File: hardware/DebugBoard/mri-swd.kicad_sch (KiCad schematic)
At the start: 7 parts, among them J1 Debug UART/Power, J2 Debug SWD, J5 OLED, SW1 Reset, SW2 Halt on Connect, U1 PicoW

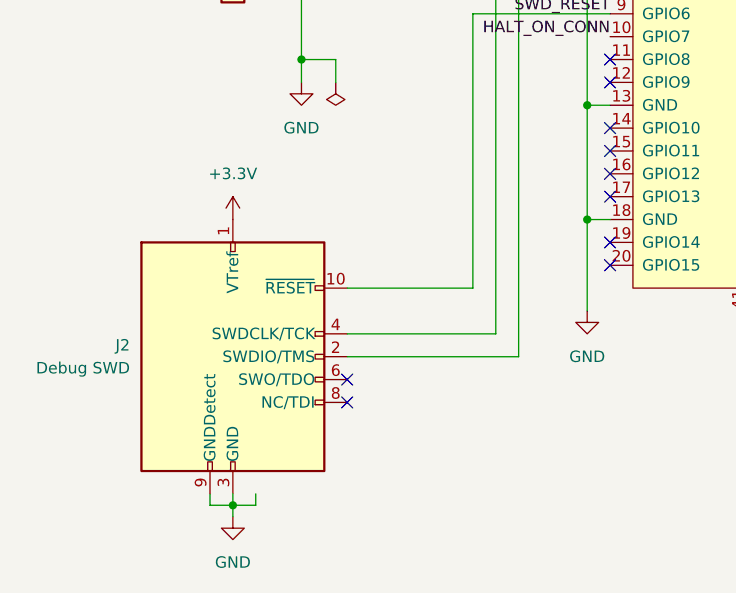
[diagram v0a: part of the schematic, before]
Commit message: Fixes to PCB found during Chomps bring up
I hit a few issues when attempting to use the mri-swd DebugBoard PCB
with the initial revision of my Chomps main board:
* The VTref pin of the SWD connector was connected to 3.3V on the debug
  board. This meant that both the target and the debugger were applying
  power to this bus. I now have the VTref pin of the SWD connector left
  unconnected. I hacked the same change into my already manufactured
  PCBs by cutting the trace leading away from the VTref pin.
* The nReset pin of the SWD connector is connected to the GPIO6 pin of
  the Pico with nothing else. This meant that nReset was connected to
  ground via the default ~50kohm pulldown of the debugger's RP2040
  and also pulled up by the default ~50kohm pull-up of the target's
  RP2040 so the voltage sits pretty close to the transition area which
  causes very weird behavior in the target and the debugger fails to
  successfully connect to the target via SWD. I added an external
  1kohm pull-up resistor to the debugger board to override the
  default pulldown behavior of the RP2040. I hacked the same change into
  my already manufactured PCBs by bodging in a 1kohm through hole
  resistor between the Pico's GPIO6 and 3.3V pins.

I bumped the version of the schematic and PCB up to 1.1 after these
changes were applied.
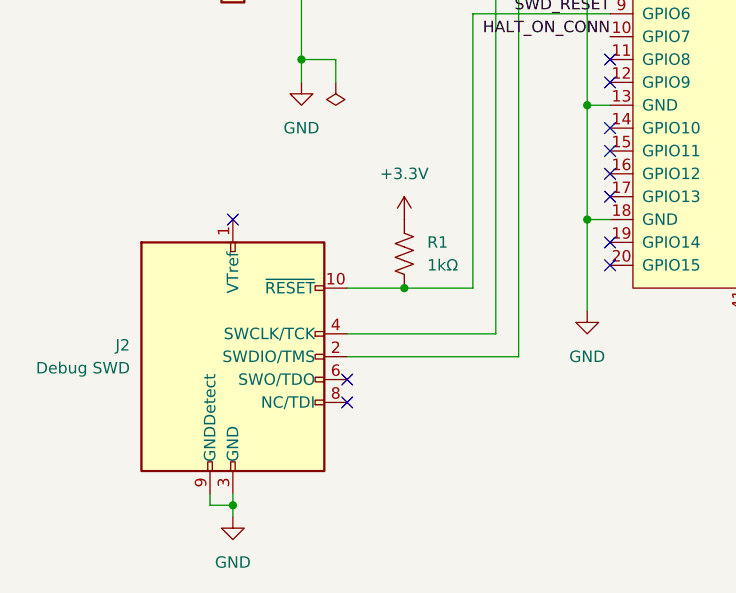
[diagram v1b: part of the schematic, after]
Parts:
- added R1: 1kΩ, Resistor_SMD:R_0805_2012Metric_Pad1.20x1.40mm_HandSolder, symbol Device:R_US
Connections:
- net +3.3V: now also R1.1; no longer J2.1 (VTref)
- net SWD_RESET: now also R1.2
- no-connect marks 25 -> 26

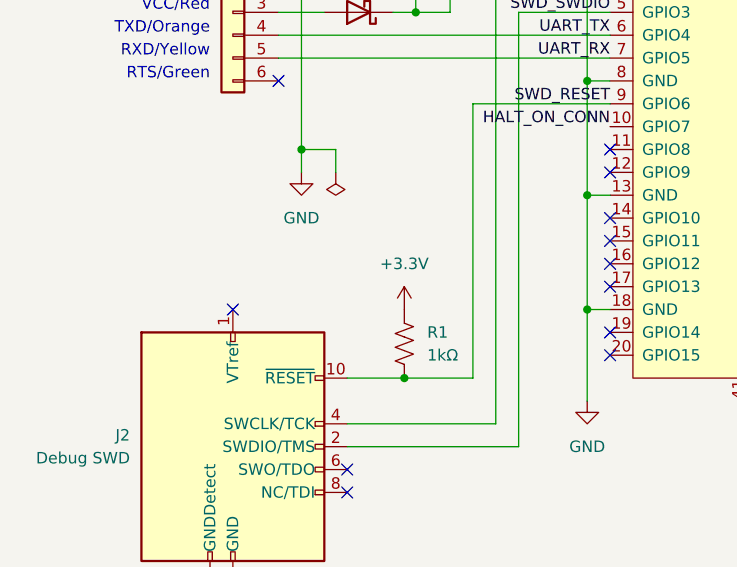
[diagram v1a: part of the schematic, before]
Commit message: More fixes to PCB found during Chomps bring up
I hit another issue when attempting to use the mri-swd DebugBoard PCB
with the initial revision of my Chomps main board:
* I previously added a 1kohm pull-up resistor to the nReset pin on the
  SWD connector but I connected it to the regulated 3.3V on the
  debugger board rather than the VTref pin on the SWD connector. This
  means that nReset wasn't pulled-up correctly if the debugger board
  wasn't powered up. Now it does the right thing even if the debugger
  board is connected to a target but hasn't been yet powered up.

I bumped the version of the schematic and PCB up to 1.2 after these
changes were applied.
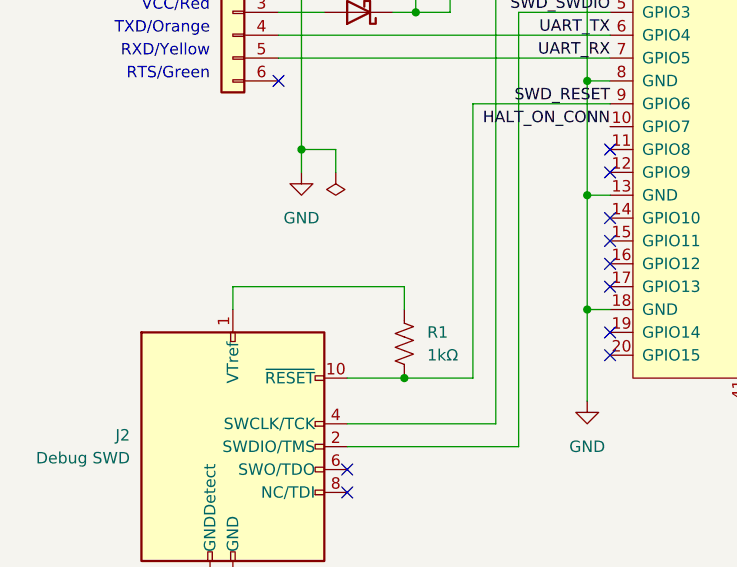
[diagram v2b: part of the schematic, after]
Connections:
- net +3.3V: no longer R1.1
- net at J2.1 (VTref): now also R1.1
- no-connect marks 26 -> 25
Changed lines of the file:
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@@
 	(title_block
 		(title "MRI SWD Hardware Debugger Board")
-		(date "2024-07-13")
+		(date "2024-07-28")
 		(rev "1.1")
 	)
@@
 		(at 147.32 90.17)
 	)
-	(no_connect
-		(at 69.85 100.33)
-	)
 	(wire
 		(pts
@@
 	(wire
 		(pts
+			(xy 69.85 100.33) (xy 69.85 97.79)
+		)
+		(stroke
+			(width 0)
+			(type default)
+		)
+	)
+	(wire
+		(pts
 			(xy 101.6 67.31) (xy 111.76 67.31)
 		)
@@
 		(pts
 			(xy 149.86 74.93) (xy 149.86 87.63)
+		)
+		(stroke
+			(width 0)
+			(type default)
+		)
+	)
+	(wire
+		(pts
+			(xy 88.9 97.79) (xy 88.9 100.33)
+		)
+		(stroke
+			(width 0)
+			(type default)
+		)
+	)
+	(wire
+		(pts
+			(xy 69.85 97.79) (xy 88.9 97.79)
 		)
 		(stroke
@@
 					(unit 1)
 				)
-			)
-		)
-	)
-	(symbol
-		(lib_id "power:+3.3V")
-		(at 88.9 100.33 0)
-		(unit 1)
-		(exclude_from_sim no)
-		(in_bom yes)
-		(on_board yes)
-		(dnp no)
-		(fields_autoplaced yes)
-		(property "Reference" "#PWR01"
-			(at 88.9 104.14 0)
-			(effects
-				(font
-					(size 1.27 1.27)
-				)
-				(hide yes)
-			)
-		)
-		(property "Value" "+3.3V"
-			(at 88.9 95.25 0)
-			(effects
-				(font
-					(size 1.27 1.27)
-				)
-			)
-		)
-		(property "Footprint" ""
-			(at 88.9 100.33 0)
-			(effects
-				(font
-					(size 1.27 1.27)
-				)
-				(hide yes)
-			)
-		)
-		(property "Datasheet" ""
-			(at 88.9 100.33 0)
-			(effects
-				(font
-					(size 1.27 1.27)
-				)
-				(hide yes)
-			)
-		)
-		(property "Description" "Power symbol creates a global label with name \"+3.3V\""
-			(at 88.9 100.33 0)
-			(effects
-				(font
-					(size 1.27 1.27)
-				)
-				(hide yes)
-			)
-		)
-		(pin "1"
-		)
-		(instances
-			(project "mri-swd"
-				(path "/80546db7-330b-449d-80f0-c8e0b594e123"
-					(reference "#PWR01")
-					(unit 1)
-				)
